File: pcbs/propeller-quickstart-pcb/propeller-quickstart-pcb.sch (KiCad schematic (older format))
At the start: 6 parts

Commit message: First version of the PCB
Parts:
- added C1: 1uF, Capacitor_THT:C_Radial_D5.0mm_H5.0mm_P2.00mm, symbol Device:C
- J1: renamed from J?; footprint (none) -> Connector_PinHeader_2.54mm:PinHeader_2x20_P2.54mm_Vertical
- U1, U2, U3, U4: renamed from U?; footprint vtx-scanner:RX5808 -> deets:RX5808
- U5: renamed from U?; footprint (none) -> Package_DIP:DIP-16_W7.62mm
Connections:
- net RCT_CLK is gone; now on net RTC_CLK: U4.6 (CLOCK/CH3)
- net +3V3: now also J1.38 (+3.3V), C1.2
- net +5V: now also J1.40 (Vin)
- net GND: now also J1.39 (GND), C1.1
- no-connect marks 24 -> 44
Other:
- moved on the sheet: U5

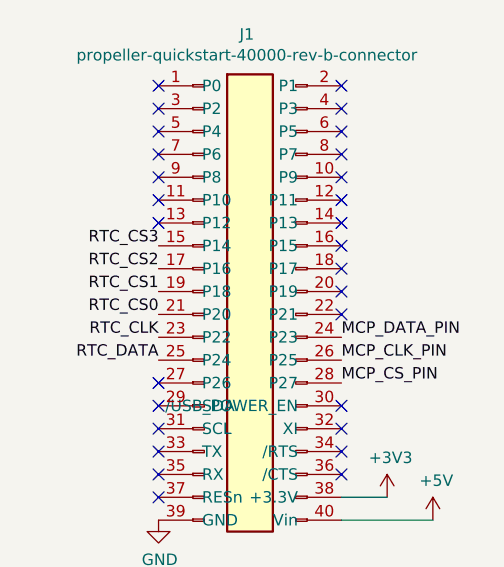
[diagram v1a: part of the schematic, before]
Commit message: Add I2C and fake mcp button
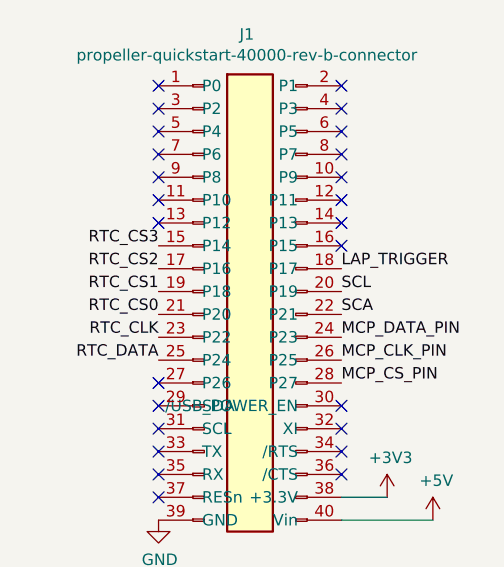
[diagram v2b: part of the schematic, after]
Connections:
- net LAP_TRIGGER: now reaches J1.18 (P17)
- net SCL: now reaches J1.20 (P19)
- net SCA: now reaches J1.22 (P21)
- no-connect marks 44 -> 41
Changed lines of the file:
@@
 NoConn ~ 7650 2900
 NoConn ~ 7650 3000
-NoConn ~ 7650 3100
-NoConn ~ 7650 3200
-NoConn ~ 7650 3300
 $Comp
 L power:GND #PWR0101
@@
 Wire Wire Line
 	5150 1800 4800 1800
+Text Label 7650 3300 0    50   ~ 0
+SCA
+Text Label 7650 3200 0    50   ~ 0
+SCL
+Text Label 7650 3100 0    50   ~ 0
+LAP_TRIGGER
 $EndSCHEMATC

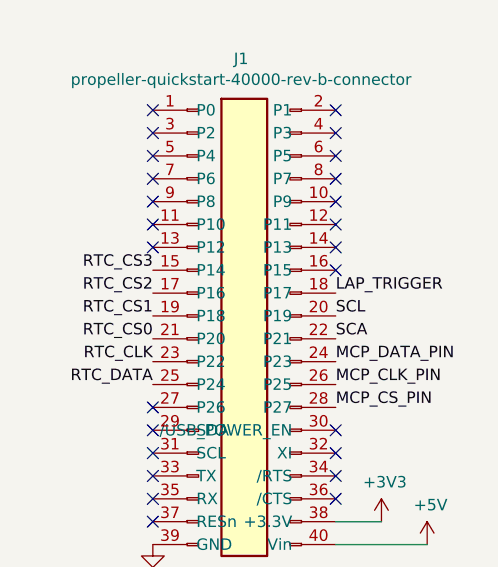
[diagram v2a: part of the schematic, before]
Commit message: Add two lines to allow for SPI
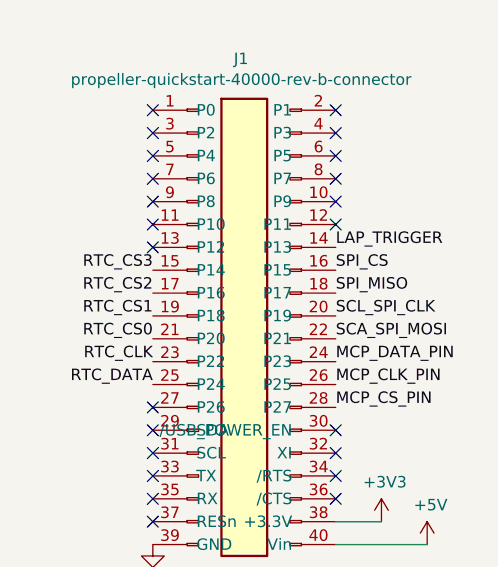
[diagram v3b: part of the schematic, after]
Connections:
- net LAP_TRIGGER: now also J1.14 (P13); no longer J1.18 (P17)
- net SPI_CS: now reaches J1.16 (P15)
- net SCA renamed SCA_SPI_MOSI
- net SCL renamed SCL_SPI_CLK
- new net SPI_MISO: J1.18 (P17)
- no-connect marks 41 -> 39
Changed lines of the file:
@@
 NoConn ~ 7650 2700
 NoConn ~ 7650 2800
-NoConn ~ 7650 2900
-NoConn ~ 7650 3000
 $Comp
 L power:GND #PWR0101
@@
 	5150 1800 4800 1800
 Text Label 7650 3300 0    50   ~ 0
-SCA
+SCA_SPI_MOSI
 Text Label 7650 3200 0    50   ~ 0
-SCL
+SCL_SPI_CLK
+Text Label 7650 2900 0    50   ~ 0
+LAP_TRIGGER
+Text Label 7650 3000 0    50   ~ 0
+SPI_CS
 Text Label 7650 3100 0    50   ~ 0
-LAP_TRIGGER
+SPI_MISO
 $EndSCHEMATC
